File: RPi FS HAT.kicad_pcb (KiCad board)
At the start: 2 copper layers, 2.8 x 2.8 mm, 7 parts, among them J1 Raspberry_Pi_2_3, SW1 SW_DPST, U1 DHT22

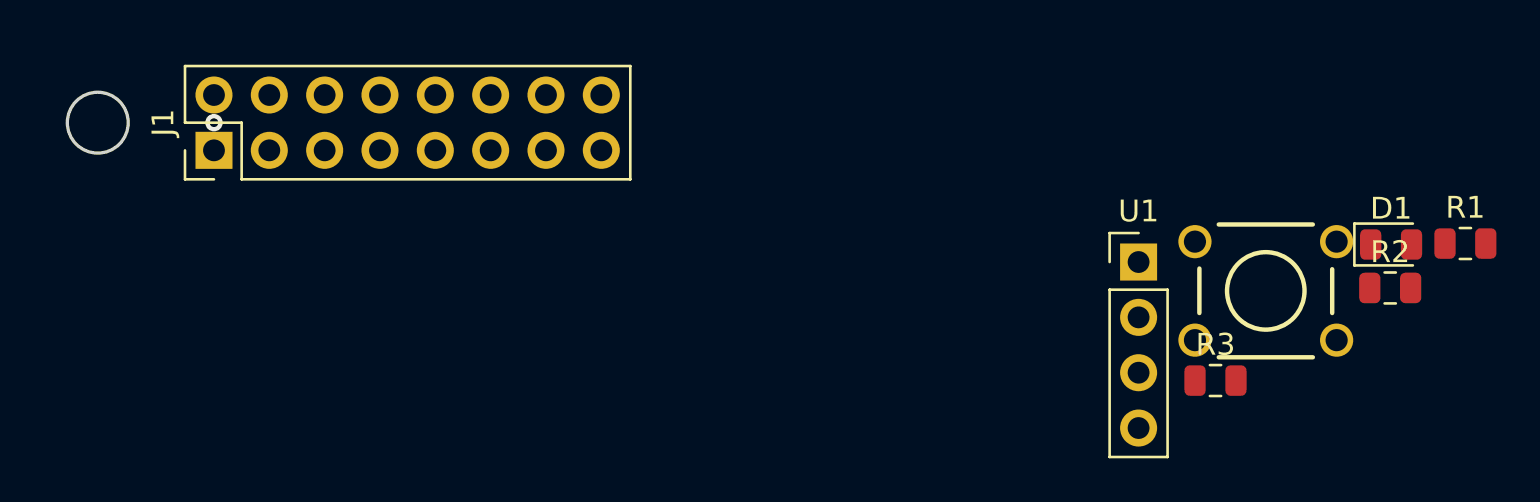
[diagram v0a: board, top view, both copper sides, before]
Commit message: Outline with rounded corners.
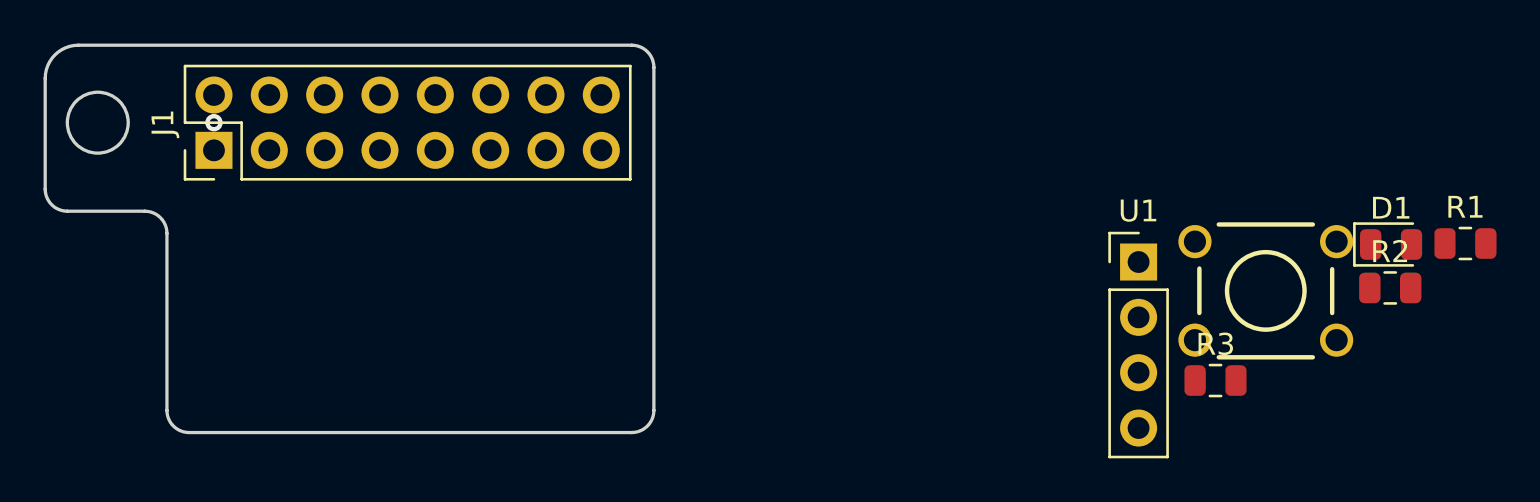
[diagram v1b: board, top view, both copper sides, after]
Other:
- board size 2.8 x 2.8 mm -> 27.9 x 17.8 mm
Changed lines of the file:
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@@
   (general
     (thickness 1.6)
-    (drawings 1)
+    (drawings 13)
     (tracks 1)
     (zones 0)
@@
     )
   )
+  (gr_line (start 168.148 114.3) (end 168.148 130.048) (layer Edge.Cuts) (width 0.15))
+  (gr_line (start 146.812 131.064) (end 167.132 131.064) (layer Edge.Cuts) (width 0.15))
+  (gr_line (start 145.796 121.92) (end 145.796 130.048) (layer Edge.Cuts) (width 0.15))
+  (gr_line (start 141.224 120.904) (end 144.78 120.904) (layer Edge.Cuts) (width 0.15))
+  (gr_line (start 140.208 114.808) (end 140.208 119.888) (layer Edge.Cuts) (width 0.15))
+  (gr_line (start 167.132 113.284) (end 141.732 113.284) (layer Edge.Cuts) (width 0.15))
+  (gr_arc (start 167.132 114.3) (end 168.148 114.3) (angle -90) (layer Edge.Cuts) (width 0.15))
+  (gr_arc (start 167.132 130.048) (end 167.132 131.064) (angle -90) (layer Edge.Cuts) (width 0.15))
+  (gr_arc (start 146.812 130.048) (end 145.796 130.048) (angle -90) (layer Edge.Cuts) (width 0.15))
+  (gr_arc (start 144.78 121.92) (end 145.796 121.92) (angle -90) (layer Edge.Cuts) (width 0.15))
+  (gr_arc (start 141.224 119.888) (end 140.208 119.888) (angle -90) (layer Edge.Cuts) (width 0.15))
+  (gr_arc (start 141.732 114.808) (end 141.732 113.284) (angle -90) (layer Edge.Cuts) (width 0.15))
   (gr_circle (center 142.621 116.84) (end 141.224 116.84) (layer Edge.Cuts) (width 0.15))
   (via (at 147.955 116.84) (size 0.8) (drill 0.4) (layers F.Cu B.Cu) (net 0))

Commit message: Footprints placed.
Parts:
- moved R1 54.0 mm to (151.4, 122.4)
- moved R2 45.5 mm to (156.5, 122.4)
- moved SW1 45.5 mm to (150.9, 127.5)
- moved D1 36.4 mm to (165.6, 122.4)
- moved R3 33.5 mm to (161.0, 122.4)
- moved U1 25.5 mm to (165.6, 129.0), turned to 270 degrees
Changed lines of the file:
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@@
   )
   (module LED_SMD:LED_0805_2012Metric (layer F.Cu)
-    (at 201.987001 122.432001)
+    (at 165.608 122.428)
     (descr "LED SMD 0805 (2012 Metric), square (rectangular) end terminal, IPC_7351 nominal, (Body size source: https://docs.google.com/spreadsheets/d/1BsfQQcO9C6DZCsRaXUlFlo91Tg2WpOkGARC1WS5S8t0/edit?usp=sharing), generated with kicad-footprint-generator")
     (tags diode)
@@
   )
   (module Resistor_SMD:R_0805_2012Metric (layer F.Cu)
-    (at 205.397001 122.387001)
+    (at 151.384 122.428)
     (descr "Resistor SMD 0805 (2012 Metric), square (rectangular) end terminal, IPC_7351 nominal, (Body size source: https://docs.google.com/spreadsheets/d/1BsfQQcO9C6DZCsRaXUlFlo91Tg2WpOkGARC1WS5S8t0/edit?usp=sharing), generated with kicad-footprint-generator")
     (tags resistor)
@@
   )
   (module Resistor_SMD:R_0805_2012Metric (layer F.Cu)
-    (at 201.947001 124.427001)
+    (at 156.464 122.428)
     (descr "Resistor SMD 0805 (2012 Metric), square (rectangular) end terminal, IPC_7351 nominal, (Body size source: https://docs.google.com/spreadsheets/d/1BsfQQcO9C6DZCsRaXUlFlo91Tg2WpOkGARC1WS5S8t0/edit?usp=sharing), generated with kicad-footprint-generator")
     (tags resistor)
@@
   )
   (module Resistor_SMD:R_0805_2012Metric (layer F.Cu)
-    (at 193.927001 128.677001)
+    (at 161.036 122.428)
     (descr "Resistor SMD 0805 (2012 Metric), square (rectangular) end terminal, IPC_7351 nominal, (Body size source: https://docs.google.com/spreadsheets/d/1BsfQQcO9C6DZCsRaXUlFlo91Tg2WpOkGARC1WS5S8t0/edit?usp=sharing), generated with kicad-footprint-generator")
     (tags resistor)
@@
   )
   (module freetronics_footprints:SW_PUSHBUTTON_PTH (layer F.Cu)
-    (at 196.2352 124.561601)
+    (at 150.876 127.508)
     (descr "<b>OMRON SWITCH</b>")
-    (fp_text reference SW1 (at -0.05 0) (layer Eco1.User)
+    (fp_text reference SW1 (at 0 0) (layer Eco1.User)
       (effects (font (size 0.6 0.6) (thickness 0.1)))
     )
@@
   )
   (module Connector_PinHeader_2.54mm:PinHeader_1x04_P2.54mm_Vertical (layer F.Cu)
-    (at 190.397001 123.237001)
+    (at 165.608 129.032 270)
     (descr "Through hole straight pin header, 1x04, 2.54mm pitch, single row")
     (tags "Through hole pin header THT 1x04 2.54mm single row")
-    (fp_text reference U1 (at 0 -2.33) (layer F.SilkS)
-      (effects (font (size 1 1) (thickness 0.15)))
-    )
-    (fp_text value DHT22 (at 0 9.95) (layer F.Fab)
+    (fp_text reference U1 (at 0 -2.33 270) (layer F.SilkS)
+      (effects (font (size 1 1) (thickness 0.15)))
+    )
+    (fp_text value DHT22 (at 0 9.95 270) (layer F.Fab)
       (effects (font (size 1 1) (thickness 0.15)))
     )
@@
     (fp_line (start 1.8 9.4) (end 1.8 -1.8) (layer F.CrtYd) (width 0.05))
     (fp_line (start 1.8 -1.8) (end -1.8 -1.8) (layer F.CrtYd) (width 0.05))
-    (fp_text user %R (at 0 3.81 90) (layer F.Fab)
-      (effects (font (size 1 1) (thickness 0.15)))
-    )
-    (pad 1 thru_hole rect (at 0 0) (size 1.7 1.7) (drill 1) (layers *.Cu *.Mask)
-      (net 3 /3V3))
-    (pad 2 thru_hole oval (at 0 2.54) (size 1.7 1.7) (drill 1) (layers *.Cu *.Mask)
+    (fp_text user %R (at 0 3.81) (layer F.Fab)
+      (effects (font (size 1 1) (thickness 0.15)))
+    )
+    (pad 1 thru_hole rect (at 0 0 270) (size 1.7 1.7) (drill 1) (layers *.Cu *.Mask)
+      (net 3 /3V3))
+    (pad 2 thru_hole oval (at 0 2.54 270) (size 1.7 1.7) (drill 1) (layers *.Cu *.Mask)
       (net 11 /sensor_data))
-    (pad 3 thru_hole oval (at 0 5.08) (size 1.7 1.7) (drill 1) (layers *.Cu *.Mask))
-    (pad 4 thru_hole oval (at 0 7.62) (size 1.7 1.7) (drill 1) (layers *.Cu *.Mask)
+    (pad 3 thru_hole oval (at 0 5.08 270) (size 1.7 1.7) (drill 1) (layers *.Cu *.Mask))
+    (pad 4 thru_hole oval (at 0 7.62 270) (size 1.7 1.7) (drill 1) (layers *.Cu *.Mask)
       (net 1 GND))
     (model ${KISYS3DMOD}/Connector_PinHeader_2.54mm.3dshapes/PinHeader_1x04_P2.54mm_Vertical.wrl
